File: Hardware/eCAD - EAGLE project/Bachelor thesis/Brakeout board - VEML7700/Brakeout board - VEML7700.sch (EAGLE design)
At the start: 5 parts, among them IC1 VEML7700-TR

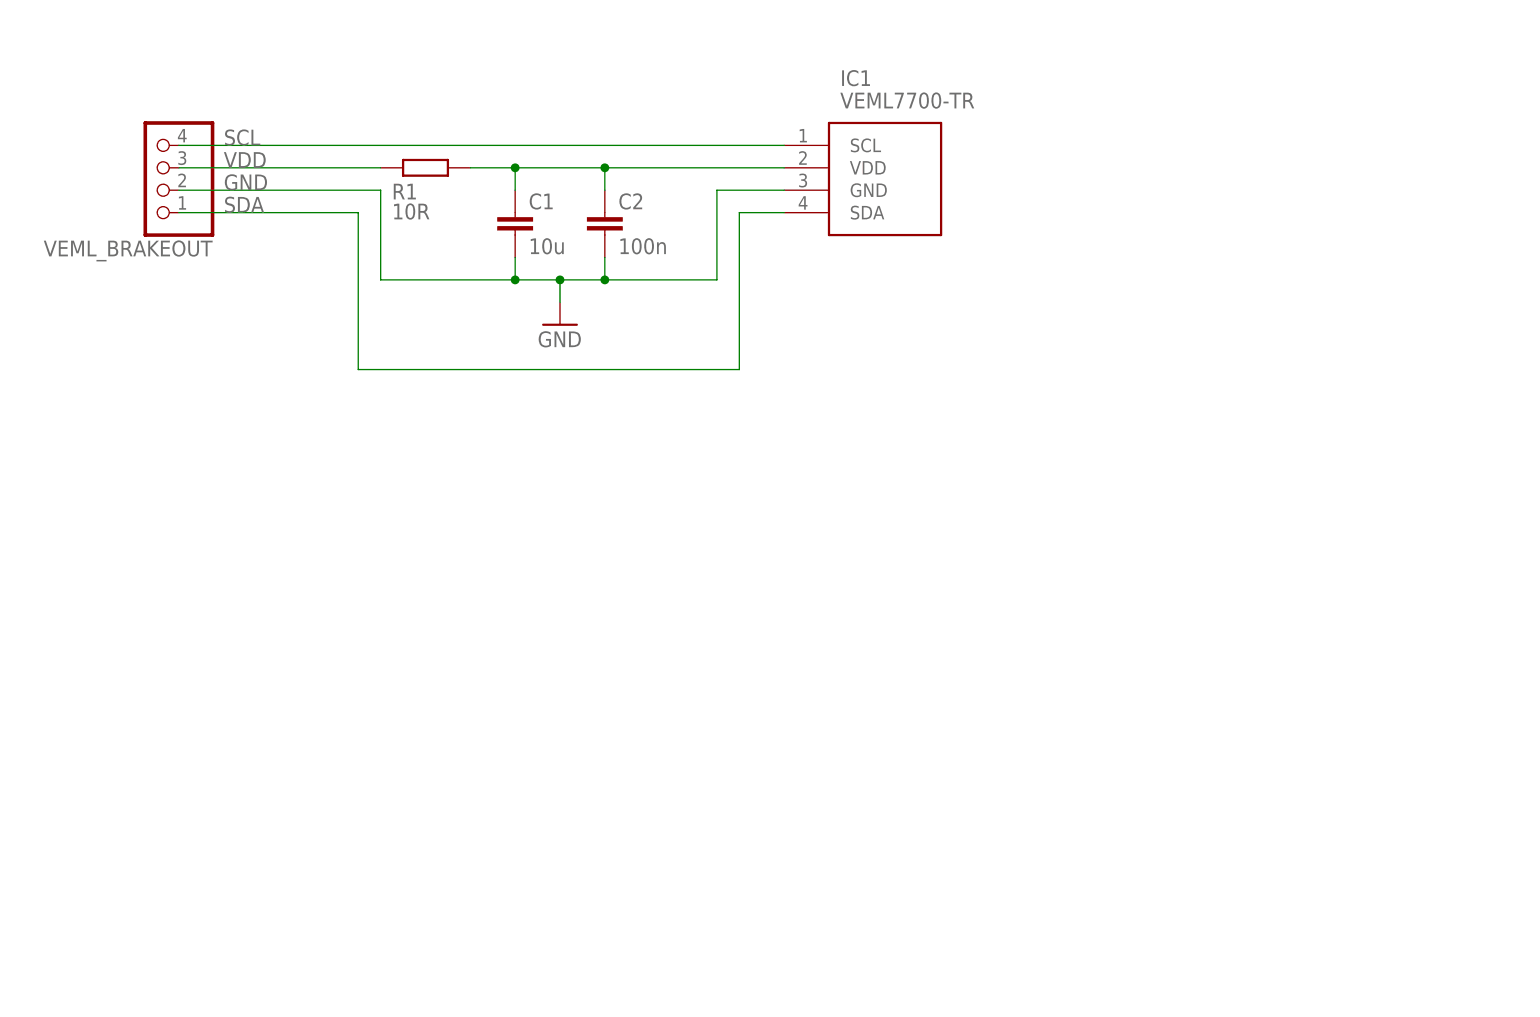
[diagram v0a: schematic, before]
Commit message: Reorder of files, added 3D models and NodeRED flow
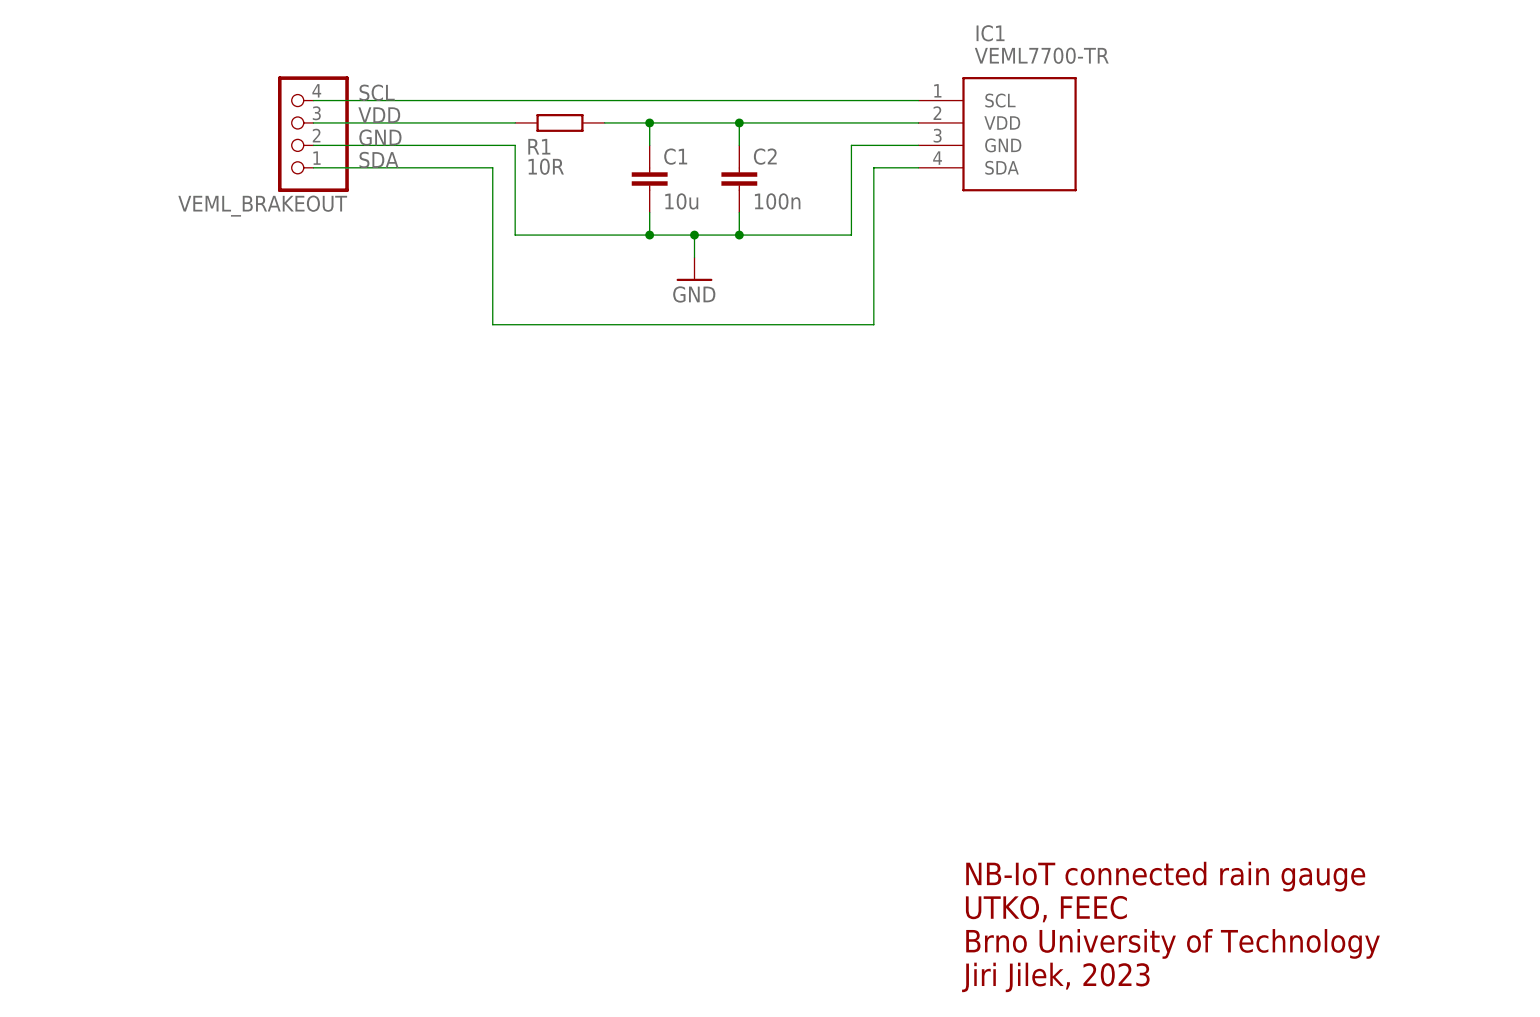
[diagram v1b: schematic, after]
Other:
- note added: "NB-IoT connected rain gauge UTKO, FEEC Brno University of Technology Jiri Jilek, 2023"
- moved on the sheet: C1, C2, IC1, R1, VEML_BRAKEOUT
